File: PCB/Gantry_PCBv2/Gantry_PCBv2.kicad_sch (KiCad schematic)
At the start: 169 parts, among them J1 Screw_Terminal_01x02, J10 B2B-XH-A_LF__SN_, J11 USB_C_Receptacle_USB2.0_16P, J12 Conn_01x04_Pin, J13 Conn_01x04_Pin, J14 Conn_01x04_Pin, J15 Conn_01x04_Pin, J16 Conn_01x05_Pin, J17 Conn_01x05_Pin, J2 DCJ200-10-A-XX-X_REVA, J3 Conn_01x03_Pin, J4 Conn_01x14, J5 B2B-XH-A_LF__SN_, J6 B2B-XH-A_LF__SN_, J7 B2B-XH-A_LF__SN_, J8 Conn_01x14, J9 Conn_01x10, Q1 NMOS, Q2 SS8050, Q3 SS8050, SW1 SW_0, SW2 SW_EN, SW3 SW_Push_DPDT, SW4 SW_Push_DPDT, SW5 SW_Push_DPDT, SW6 SW_Push_DPDT, U10 74HC245, U11 74HC245, U12 MCP23017_SO, U13 CP2102N-Axx-xQFN28, U14 ESP32-WROOM-32U, U2 MP1584, U4 TLV75733PDBV, U5 DRV8825_STEPPER_MOTOR_DRIVER_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, U6 DRV8825_STEPPER_MOTOR_DRIVER_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, U7 TB6612FNG H-bridge Motor Driv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, U8 DRV8825_STEPPER_MOTOR_DRIVER_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, U9 DRV8825_STEPPER_MOTOR_DRIVER_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

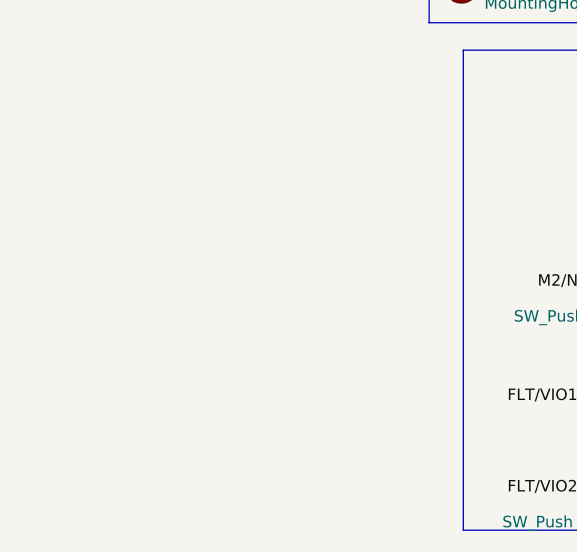
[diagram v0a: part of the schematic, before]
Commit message: Added Octal Bus Symbol
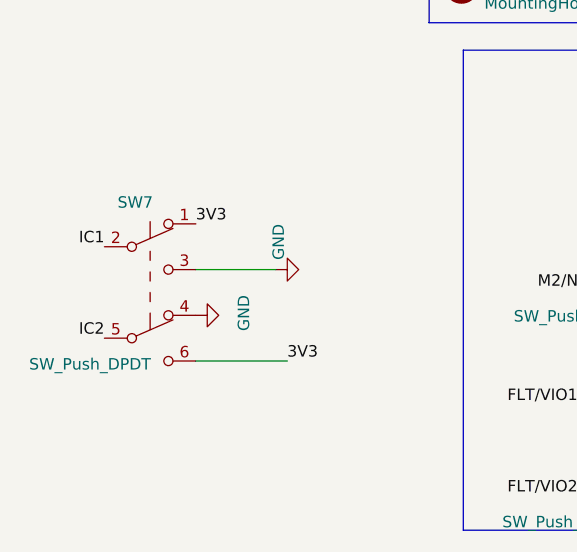
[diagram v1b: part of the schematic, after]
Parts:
- added SW7: SW_Push_DPDT, dpdt_tht:dpdt, symbol Switch:SW_Push_DPDT
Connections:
- net 3V3: now also SW7.1 (A), SW7.6 (C)
- net GND: now also SW7.3 (C), SW7.4 (A)
- new net IC1: SW7.2 (B)
- new net IC2: SW7.5 (B)

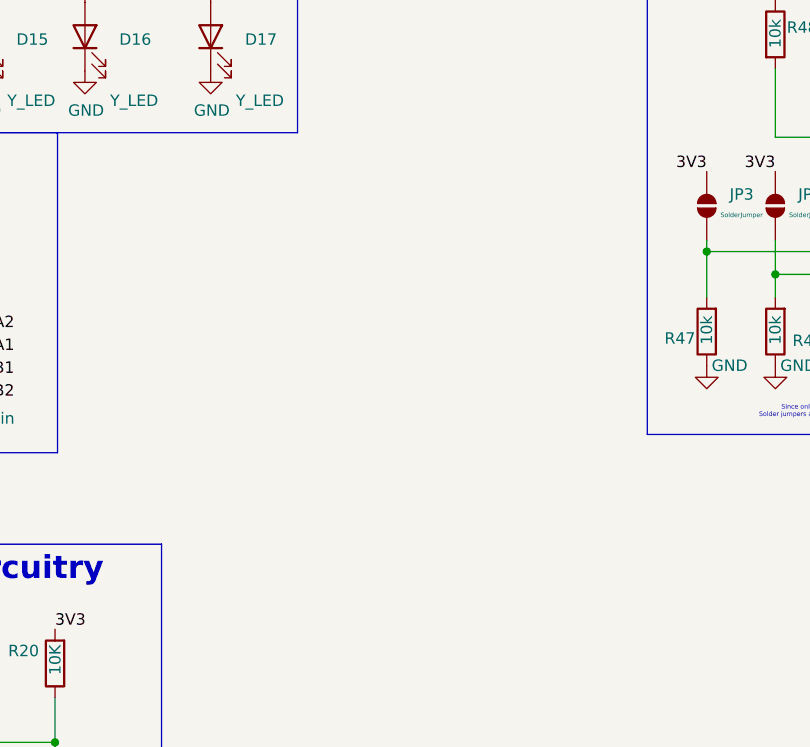
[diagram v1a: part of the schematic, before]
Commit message: Final symbol for Switch Bus
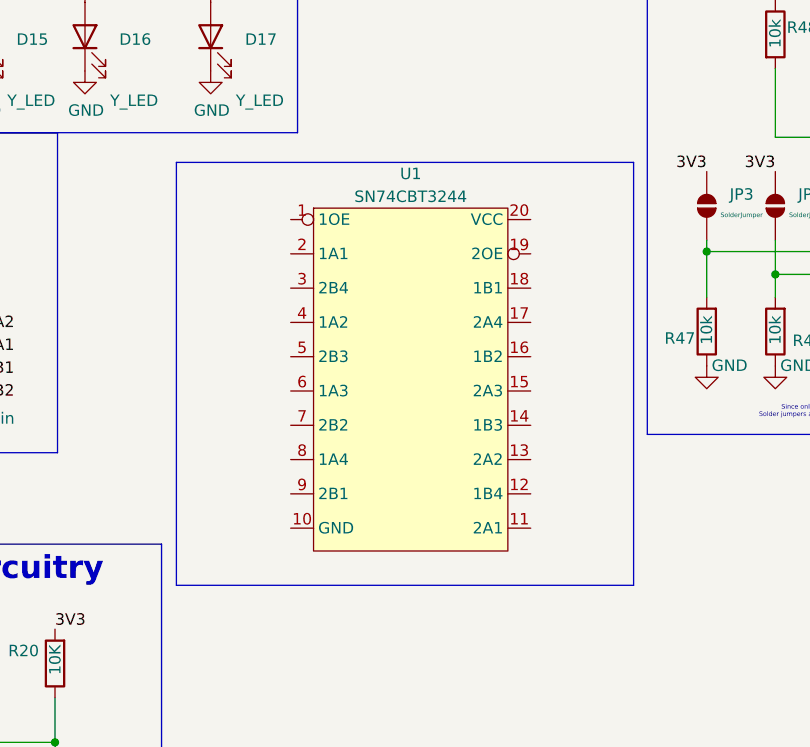
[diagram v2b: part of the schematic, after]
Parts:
- added U1: SN74CBT3244, symbol Gantry:SN74CBT3244
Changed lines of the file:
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@@
 	)
 	(rectangle
+		(start 292.1 251.46)
+		(end 342.9 298.45)
+		(stroke
+			(width 0)
+			(type default)
+		)
+		(fill
+			(type none)
+		)
+	)
+	(rectangle
 		(start 163.068 92.456)
 		(end 344.424 201.93)
@@
 					(unit 1)
 				)
+			)
+		)
+	)
+	(symbol
+		(lib_id "Gantry:SN74CBT3244")
+		(at 308.61 257.81 0)
+		(unit 1)
+		(exclude_from_sim no)
+		(in_bom yes)
+		(on_board yes)
+		(dnp no)
+		(fields_autoplaced yes)
+		(property "Reference" "U1"
+			(at 318.135 252.73 0)
+			(effects
+				(font
+					(size 1.27 1.27)
+				)
+			)
+		)
+		(property "Value" "SN74CBT3244"
+			(at 318.135 255.27 0)
+			(effects
+				(font
+					(size 1.27 1.27)
+				)
+			)
+		)
+		(property "Footprint" ""
+			(at 308.61 257.81 0)
+			(effects
+				(font
+					(size 1.27 1.27)
+				)
+				(hide yes)
+			)
+		)
+		(property "Datasheet" ""
+			(at 308.61 257.81 0)
+			(effects
+				(font
+					(size 1.27 1.27)
+				)
+				(hide yes)
+			)
+		)
+		(property "Description" ""
+			(at 308.61 257.81 0)
+			(effects
+				(font
+					(size 1.27 1.27)
+				)
+				(hide yes)
+			)
+		)
+		(pin "4"
+		)
+		(pin "16"
+		)
+		(pin "10"
+		)
+		(pin "2"
+		)
+		(pin "11"
+		)
+		(pin "15"
+		)
+		(pin "8"
+		)
+		(pin "1"
+		)
+		(pin "13"
+		)
+		(pin "20"
+		)
+		(pin "12"
+		)
+		(pin "17"
+		)
+		(pin "18"
+		)
+		(pin "6"
+		)
+		(pin "14"
+		)
+		(pin "9"
+		)
+		(pin "7"
+		)
+		(pin "5"
+		)
+		(pin "3"
+		)
+		(pin "19"
+		)
+		(instances
+			(project ""
+				(path "/e63e39d7-6ac0-4ffd-8aa3-1841a4541b55"
+					(reference "U1")
+					(unit 1)
+				)

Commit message: Completed Bus Schematic, Added Labels and Rounded the Tracks
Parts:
- removed SW5, SW6, SW7: SW_Push_DPDT, dpdt_tht:dpdt, symbol Switch:SW_Push_DPDT
- U1: footprint (none) -> Package_SO:TSSOP-20_4.4x5mm_P0.5mm
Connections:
- net 3V3: now also SW3.1 (A), U1.2 (1A1), U1.4 (1A2), U1.6 (1A3), U1.8 (1A4)
- net 5V_R: now also U1.20 (VCC)
- net FLT/VIO1: now also TP9.1, U1.18 (1B1)
- net FLT/VIO2: now also TP10.1, U1.16 (1B2)
- net FLT/VIO3: now also TP11.1, U1.14 (1B3)
- net FLT/VIO4: now also TP12.1, U1.12 (1B4)
- net GND: now also SW3.3 (C), U1.10 (GND)
- net IC1: now also SW3.2 (B), U1.1 (1OE)
- no-connect marks 40 -> 37
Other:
- moved on the sheet: C10, C11, C12, C13, C14, C15, C16, C17, C18, C19, C2, C20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
